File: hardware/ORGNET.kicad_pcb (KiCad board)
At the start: 2 copper layers, 21 x 50 mm, 41 parts, among them J1 Conn_02x08_Odd_Even, J3 Conn_01x03, U1 SN74LVC8T245, U2 SN74LVC8T245, U3 AP2112K-3.3, U4 RP2350A, U5 W25Q128JVP, U6 Raspberry Pi Radio Module 2, Y1 12M

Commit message: Add logo and branding to PCB
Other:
- board text added: "Affix magical futuristic high-speed radio module here"
- board text added: "MADE IN UK"
- board text added: "V1"
- board text added: "Wireless networking pack for the Psion Organiser II"
- board text added: "orgnet.jamesl.me"

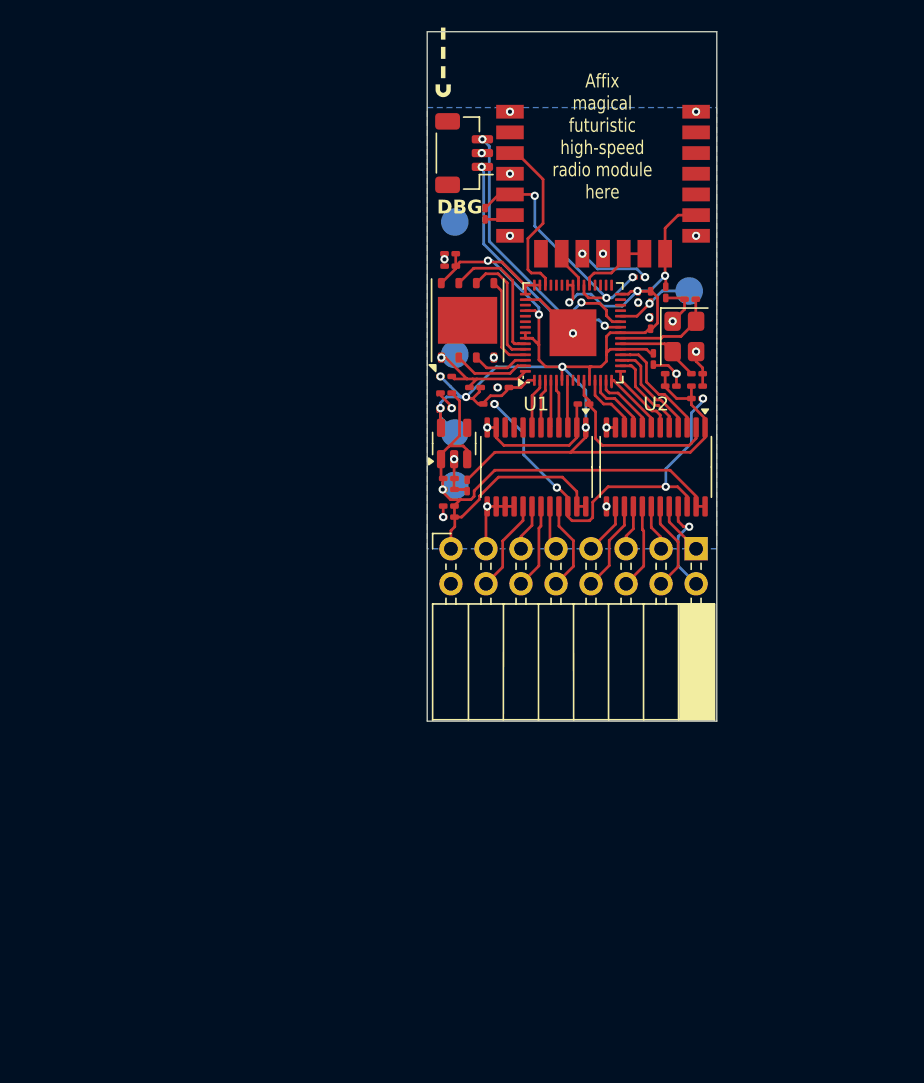
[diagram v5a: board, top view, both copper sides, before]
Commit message: Add branding to schematics
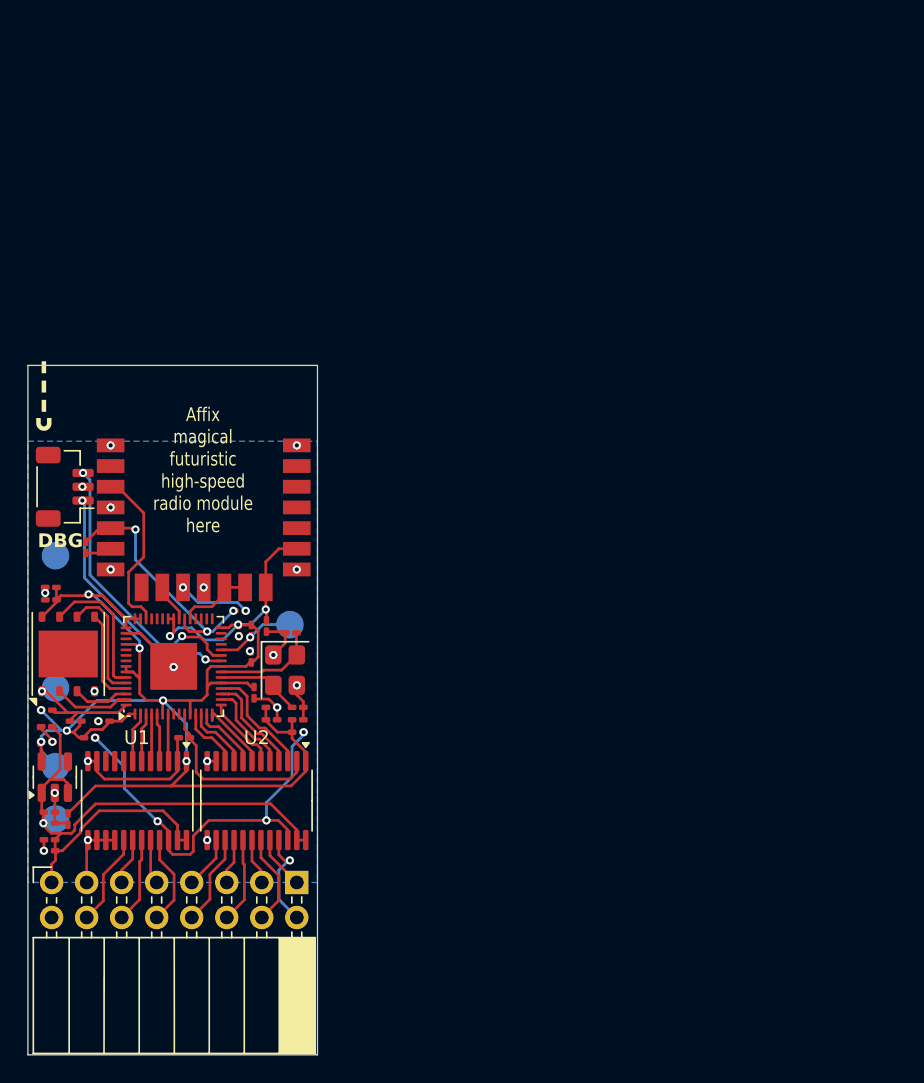
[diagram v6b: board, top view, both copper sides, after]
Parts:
- moved C1 37.7 mm to (144.9, 106.6)
- moved C12 37.7 mm to (158.4, 97.4)
- moved C14 37.7 mm to (157.3, 92.9)
- moved C16 37.7 mm to (143.7, 89.8)
- moved C18 37.7 mm to (161.6, 98.5)
- moved C3 37.7 mm to (143.6, 108.9)
- moved C4 37.7 mm to (161.6, 99.4)
- moved C6 37.7 mm to (143.6, 106.9)
- moved C7 37.7 mm to (143.4, 99.9)
- moved C8 37.7 mm to (143.4, 101.0)
- moved C9 37.7 mm to (147.6, 99.5)
- moved J1 37.7 mm to (143.8, 111.2)
- moved J3 37.7 mm to (144.7, 82.5)
- moved R1 37.7 mm to (146.5, 100.7)
- moved R2 37.7 mm to (153.4, 100.7)
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
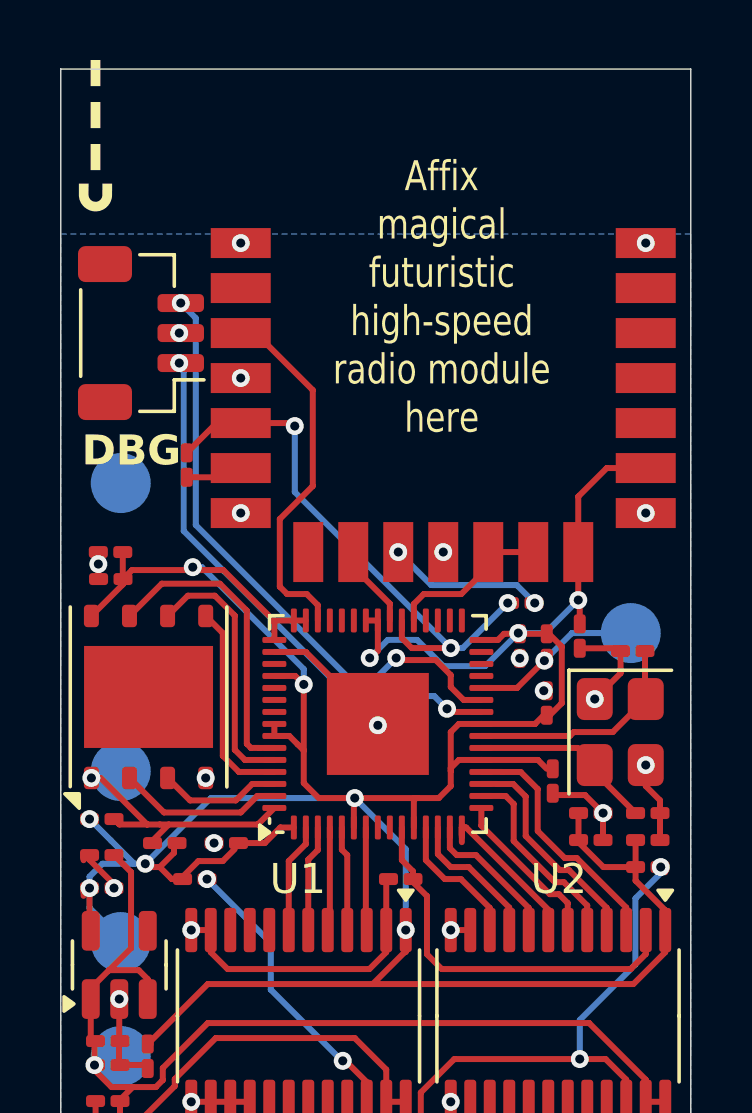
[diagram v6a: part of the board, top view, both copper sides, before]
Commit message: Make a few minor changes to PCB layout and silkscreen
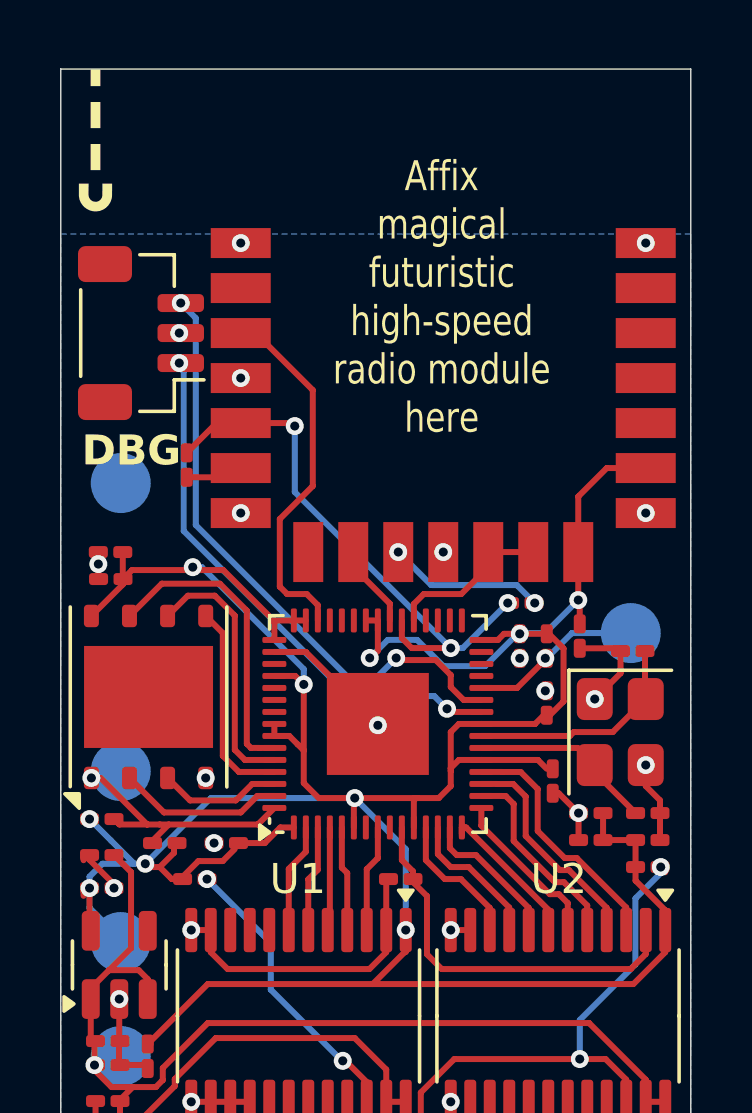
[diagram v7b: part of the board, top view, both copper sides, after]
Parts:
- moved C10 0.90 mm to (159.7, 98.5), turned to 0 degrees
- moved C11 0.90 mm to (159.7, 99.4), turned to 0 degrees
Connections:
- U4 pad 7: RP_SCLK -> unconnected-(U4-GPIO4-Pad7)
- U4 pad 8: unconnected-(U4-GPIO5-Pad8) -> RP_SCLK
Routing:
- net +3V3: track 117.8 -> 116.7 mm
- net GND: track 35.9 -> 35.2 mm
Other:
- board text added: "MADE IN U.K."
- board text removed: "MADE IN UK"

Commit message: Implement a few more minor PCB tweaks
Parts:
- C10, C11, C12, C9: value 0.1u -> 1u
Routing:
- net DBG_SWDIO: track 20.5 -> 19.8 mm
- net GND: vias 23 -> 36
- net (no net): vias 0 -> 4
